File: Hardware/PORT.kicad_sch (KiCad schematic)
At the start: 6 parts

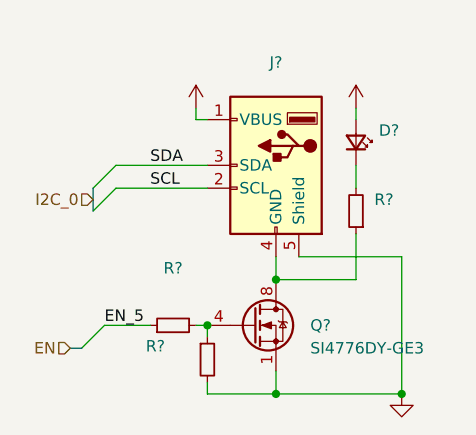
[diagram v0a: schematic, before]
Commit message: added hierrarchial labels
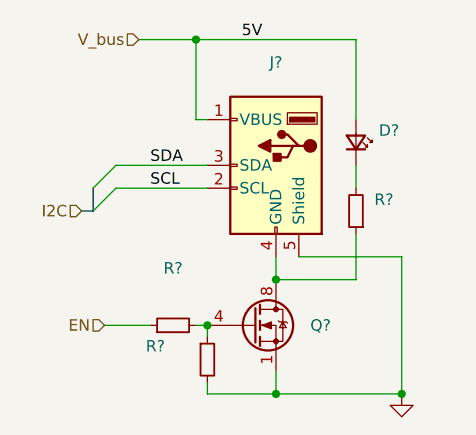
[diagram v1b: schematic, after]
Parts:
- removed D?: ~, symbol Device:LED_Small
- removed J?: ~, symbol Connector:USB_A
- removed Q?: SI4776DY-GE3, symbol Transistor_FET:Si4162DY
- removed R? (x3): ~, symbol Device:R_Small
- added D?: (no value), symbol Device:LED_Small
- added J?: (no value), symbol Connector:USB_A
- added Q?: (no value), symbol Transistor_FET:Si4162DY
- added R? (x3): (no value), symbol Device:R_Small
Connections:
- net EN: now also R?.1
- net GND: now also J?.5 (Shield), Q?.1 (S), Q?.2 (S), Q?.3 (S), R?.2
- net SCL: now also J?.2 (SCL)
- net SDA: now also J?.3 (SDA)
- new net: D?.1 (K), R?.2
- new net: Q?.4 (G), R?.1, R?.2
- new net: J?.4 (GND), Q?.5 (D), Q?.6 (D), Q?.7 (D), Q?.8 (D), R?.1
- new net V_bus: D?.2 (A), J?.1 (VBUS)
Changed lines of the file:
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@@
   (junction (at 101.6 60.96) (diameter 0) (color 0 0 0 0)
   )
+  (junction (at 92.71 34.29) (diameter 0) (color 0 0 0 0)
+  )
   (junction (at 93.98 66.04) (diameter 0) (color 0 0 0 0)
   )
@@
     (stroke (width 0) (type default) (color 0 0 0 0))
   )
-  (bus_entry (at 82.55 66.04) (size -2.54 2.54)
-    (stroke (width 0) (type default) (color 0 0 0 0))
-  )
-  (wire (pts (xy 110.49 41.91) (xy 110.49 43.18))
+  (wire (pts (xy 110.49 34.29) (xy 92.71 34.29))
+    (stroke (width 0) (type default) (color 0 0 0 0))
+  )
+  (wire (pts (xy 110.49 34.29) (xy 110.49 43.18))
     (stroke (width 0) (type default) (color 0 0 0 0))
   )
@@
     (stroke (width 0) (type default) (color 0 0 0 0))
   )
+  (wire (pts (xy 92.71 34.29) (xy 86.36 34.29))
+    (stroke (width 0) (type default) (color 0 0 0 0))
+  )
   (wire (pts (xy 101.6 73.66) (xy 115.57 73.66))
     (stroke (width 0) (type default) (color 0 0 0 0))
@@
     (stroke (width 0) (type default) (color 0 0 0 0))
   )
-  (wire (pts (xy 92.71 41.91) (xy 92.71 43.18))
+  (wire (pts (xy 92.71 34.29) (xy 92.71 43.18))
     (stroke (width 0) (type default) (color 0 0 0 0))
   )
@@
     (stroke (width 0) (type default) (color 0 0 0 0))
   )
-  (bus (pts (xy 78.74 68.58) (xy 80.01 68.58))
+  (bus (pts (xy 80.01 53.34) (xy 81.28 53.34))
     (stroke (width 0) (type default) (color 0 0 0 0))
   )
@@
     (effects (font (size 1.27 1.27)) (justify left bottom))
   )
-  (label "EN_5" (at 82.55 66.04 0)
-    (effects (font (size 1.27 1.27)) (justify left bottom))
-  )
   (label "SCL" (at 87.6284 50.8 0)
     (effects (font (size 1.27 1.27)) (justify left bottom))
   )
-  (hierarchical_label "I2C_0" (shape input) (at 81.28 52.07 180)
+  (label "5V" (at 97.79 34.29 0)
+    (effects (font (size 1.27 1.27)) (justify left bottom))
+  )
+  (hierarchical_label "V_bus" (shape input) (at 86.36 34.29 180)
     (effects (font (size 1.27 1.27)) (justify right))
   )
-  (hierarchical_label "EN" (shape input) (at 78.74 68.58 180)
+  (hierarchical_label "EN" (shape input) (at 82.55 66.04 180)
     (effects (font (size 1.27 1.27)) (justify right))
   )
-  (symbol (lib_id "power:+5V") (at 110.49 41.91 0) (unit 1)
-    (in_bom yes) (on_board yes)
-    (property "Reference" "#PWR?" (id 0) (at 110.49 45.72 0)
-      (effects (font (size 1.27 1.27)) hide)
-    )
-    (property "Value" "~" (id 1) (at 111.76 40.64 0)
-      (effects (font (size 1.27 1.27)) (justify left))
-    )
-    (property "Footprint" "" (id 2) (at 110.49 41.91 0)
-      (effects (font (size 1.27 1.27)) hide)
-    )
-    (property "Datasheet" "" (id 3) (at 110.49 41.91 0)
-      (effects (font (size 1.27 1.27)) hide)
-    )
-    (pin "1")
+  (hierarchical_label "I2C" (shape input) (at 80.01 53.34 180)
+    (effects (font (size 1.27 1.27)) (justify right))
+  )
+  (symbol (lib_id "Device:LED_Small") (at 110.49 45.72 270) (mirror x) (unit 1)
+    (in_bom yes) (on_board yes) (fields_autoplaced)
+    (property "Reference" "D?" (id 0) (at 113.03 44.3864 90)
+      (effects (font (size 1.27 1.27)) (justify left))
+    )
+    (property "Value" "" (id 1) (at 113.03 46.9264 90)
+      (effects (font (size 1.27 1.27)) (justify left))
+    )
+    (property "Footprint" "" (id 2) (at 110.49 45.72 90)
+      (effects (font (size 1.27 1.27)) hide)
+    )
+    (property "Datasheet" "~" (id 3) (at 110.49 45.72 90)
+      (effects (font (size 1.27 1.27)) hide)
+    )
+    (pin "1")
+    (pin "2")
   )
   (symbol (lib_id "Device:R_Small") (at 93.98 69.85 0) (unit 1)
@@
       (effects (font (size 1.27 1.27)) (justify left))
     )
-    (property "Value" "~" (id 1) (at 87.1354 70.8955 0)
+    (property "Value" "" (id 1) (at 87.1354 70.8955 0)
       (effects (font (size 1.27 1.27)) (justify left))
     )
@@
     (pin "2")
   )
-  (symbol (lib_id "Device:R_Small") (at 90.17 66.04 90) (unit 1)
+  (symbol (lib_id "power:GND") (at 115.57 73.66 0) (unit 1)
+    (in_bom yes) (on_board yes)
+    (property "Reference" "#PWR?" (id 0) (at 115.57 80.01 0)
+      (effects (font (size 1.27 1.27)) hide)
+    )
+    (property "Value" "" (id 1) (at 118.11 73.66 0))
+    (property "Footprint" "" (id 2) (at 115.57 73.66 0)
+      (effects (font (size 1.27 1.27)) hide)
+    )
+    (property "Datasheet" "" (id 3) (at 115.57 73.66 0)
+      (effects (font (size 1.27 1.27)) hide)
+    )
+    (pin "1")
+  )
+  (symbol (lib_id "Device:R_Small") (at 110.49 53.34 180) (unit 1)
     (in_bom yes) (on_board yes) (fields_autoplaced)
-    (property "Reference" "R?" (id 0) (at 90.17 59.69 90))
-    (property "Value" "~" (id 1) (at 90.17 62.23 90))
-    (property "Footprint" "" (id 2) (at 90.17 66.04 0)
-      (effects (font (size 1.27 1.27)) hide)
-    )
-    (property "Datasheet" "~" (id 3) (at 90.17 66.04 0)
-      (effects (font (size 1.27 1.27)) hide)
-    )
-    (pin "1")
-    (pin "2")
-  )
-  (symbol (lib_name "USB_A_1") (lib_id "Connector:USB_A") (at 101.6 48.26 0) (mirror y) (unit 1)
-    (in_bom yes) (on_board yes)
-    (property "Reference" "J?" (id 0) (at 101.6 36.83 0))
-    (property "Value" "~" (id 1) (at 101.6 39.37 0))
-    (property "Footprint" "" (id 2) (at 97.79 49.53 0)
-      (effects (font (size 1.27 1.27)) hide)
-    )
-    (property "Datasheet" " ~" (id 3) (at 97.79 49.53 0)
-      (effects (font (size 1.27 1.27)) hide)
-    )
-    (pin "1")
-    (pin "2")
-    (pin "3")
-    (pin "4")
-    (pin "5")
-  )
-  (symbol (lib_id "power:+5V") (at 92.71 41.91 0) (unit 1)
-    (in_bom yes) (on_board yes)
-    (property "Reference" "#PWR?" (id 0) (at 92.71 45.72 0)
-      (effects (font (size 1.27 1.27)) hide)
-    )
-    (property "Value" "~" (id 1) (at 86.36 40.64 0)
-      (effects (font (size 1.27 1.27)) (justify left))
-    )
-    (property "Footprint" "" (id 2) (at 92.71 41.91 0)
-      (effects (font (size 1.27 1.27)) hide)
-    )
-    (property "Datasheet" "" (id 3) (at 92.71 41.91 0)
-      (effects (font (size 1.27 1.27)) hide)
-    )
-    (pin "1")
+    (property "Reference" "R?" (id 0) (at 112.5301 52.0699 0)
+      (effects (font (size 1.27 1.27)) (justify right))
+    )
+    (property "Value" "" (id 1) (at 112.5301 54.6099 0)
+      (effects (font (size 1.27 1.27)) (justify right))
+    )
+    (property "Footprint" "" (id 2) (at 110.49 53.34 0)
+      (effects (font (size 1.27 1.27)) hide)
+    )
+    (property "Datasheet" "~" (id 3) (at 110.49 53.34 0)
+      (effects (font (size 1.27 1.27)) hide)
+    )
+    (pin "1")
+    (pin "2")
   )
   (symbol (lib_id "Transistor_FET:Si4162DY") (at 99.06 66.04 0) (unit 1)
@@
       (effects (font (size 1.27 1.27)) (justify left))
     )
-    (property "Value" "SI4776DY-GE3" (id 1) (at 105.41 68.58 0)
+    (property "Value" "" (id 1) (at 105.41 68.58 0)
       (effects (font (size 1.27 1.27)) (justify left))
     )
@@
     (pin "8")
   )
-  (symbol (lib_id "Device:R_Small") (at 110.49 53.34 180) (unit 1)
+  (symbol (lib_id "Device:R_Small") (at 90.17 66.04 90) (unit 1)
     (in_bom yes) (on_board yes) (fields_autoplaced)
-    (property "Reference" "R?" (id 0) (at 112.5301 52.0699 0)
-      (effects (font (size 1.27 1.27)) (justify right))
-    )
-    (property "Value" "~" (id 1) (at 112.5301 54.6099 0)
-      (effects (font (size 1.27 1.27)) (justify right))
-    )
-    (property "Footprint" "" (id 2) (at 110.49 53.34 0)
-      (effects (font (size 1.27 1.27)) hide)
-    )
-    (property "Datasheet" "~" (id 3) (at 110.49 53.34 0)
-      (effects (font (size 1.27 1.27)) hide)
-    )
-    (pin "1")
-    (pin "2")
-  )
-  (symbol (lib_id "power:GND") (at 115.57 73.66 0) (unit 1)
-    (in_bom yes) (on_board yes)
-    (property "Reference" "#PWR?" (id 0) (at 115.57 80.01 0)
-      (effects (font (size 1.27 1.27)) hide)
-    )
-    (property "Value" "~" (id 1) (at 118.11 73.66 0))
-    (property "Footprint" "" (id 2) (at 115.57 73.66 0)
-      (effects (font (size 1.27 1.27)) hide)
-    )
-    (property "Datasheet" "" (id 3) (at 115.57 73.66 0)
-      (effects (font (size 1.27 1.27)) hide)
-    )
-    (pin "1")
-  )
-  (symbol (lib_id "Device:LED_Small") (at 110.49 45.72 270) (mirror x) (unit 1)
-    (in_bom yes) (on_board yes) (fields_autoplaced)
-    (property "Reference" "D?" (id 0) (at 113.03 44.3864 90)
-      (effects (font (size 1.27 1.27)) (justify left))
-    )
-    (property "Value" "~" (id 1) (at 113.03 46.9264 90)
-      (effects (font (size 1.27 1.27)) (justify left))
-    )
-    (property "Footprint" "" (id 2) (at 110.49 45.72 90)
-      (effects (font (size 1.27 1.27)) hide)
-    )
-    (property "Datasheet" "~" (id 3) (at 110.49 45.72 90)
-      (effects (font (size 1.27 1.27)) hide)
-    )
-    (pin "1")
-    (pin "2")
+    (property "Reference" "R?" (id 0) (at 90.17 59.69 90))
+    (property "Value" "" (id 1) (at 90.17 62.23 90))
+    (property "Footprint" "" (id 2) (at 90.17 66.04 0)
+      (effects (font (size 1.27 1.27)) hide)
+    )
+    (property "Datasheet" "~" (id 3) (at 90.17 66.04 0)
+      (effects (font (size 1.27 1.27)) hide)
+    )
+    (pin "1")
+    (pin "2")
+  )
+  (symbol (lib_name "USB_A_1") (lib_id "Connector:USB_A") (at 101.6 48.26 0) (mirror y) (unit 1)
+    (in_bom yes) (on_board yes)
+    (property "Reference" "J?" (id 0) (at 101.6 36.83 0))
+    (property "Value" "" (id 1) (at 101.6 39.37 0))
+    (property "Footprint" "" (id 2) (at 97.79 49.53 0)
+      (effects (font (size 1.27 1.27)) hide)
+    )
+    (property "Datasheet" " ~" (id 3) (at 97.79 49.53 0)
+      (effects (font (size 1.27 1.27)) hide)
+    )
+    (pin "1")
+    (pin "2")
+    (pin "3")
+    (pin "4")
+    (pin "5")
   )
 )

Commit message: cleaned up busses
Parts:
- D?: value (none) -> GLED
- J?: value (none) -> USB
- Q?: value (none) -> SI4776DY-GE3
- R?: value (none) -> 1Meg
- R? (x2): value (none) -> 1k
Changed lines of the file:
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@@
   (junction (at 101.6 73.66) (diameter 0) (color 0 0 0 0)
-  )
-  (bus_entry (at 83.82 48.26) (size -2.54 2.54)
-    (stroke (width 0) (type default) (color 0 0 0 0))
-  )
-  (bus_entry (at 83.82 50.8) (size -2.54 2.54)
-    (stroke (width 0) (type default) (color 0 0 0 0))
   )
   (wire (pts (xy 110.49 34.29) (xy 92.71 34.29))
@@
     (stroke (width 0) (type default) (color 0 0 0 0))
   )
-  (bus (pts (xy 80.01 53.34) (xy 81.28 53.34))
-    (stroke (width 0) (type default) (color 0 0 0 0))
-  )
   (wire (pts (xy 82.55 66.04) (xy 87.63 66.04))
     (stroke (width 0) (type default) (color 0 0 0 0))
@@
   )
   (wire (pts (xy 110.49 60.96) (xy 101.6 60.96))
-    (stroke (width 0) (type default) (color 0 0 0 0))
-  )
-  (bus (pts (xy 81.28 50.8) (xy 81.28 53.34))
     (stroke (width 0) (type default) (color 0 0 0 0))
   )
@@
     (effects (font (size 1.27 1.27)) (justify right))
   )
+  (hierarchical_label "SCL" (shape input) (at 83.82 50.8 180)
+    (effects (font (size 1.27 1.27)) (justify right))
+  )
   (hierarchical_label "EN" (shape input) (at 82.55 66.04 180)
     (effects (font (size 1.27 1.27)) (justify right))
   )
-  (hierarchical_label "I2C" (shape input) (at 80.01 53.34 180)
+  (hierarchical_label "SDA" (shape input) (at 83.82 48.26 180)
     (effects (font (size 1.27 1.27)) (justify right))
   )
@@
       (effects (font (size 1.27 1.27)) (justify left))
     )
-    (property "Value" "" (id 1) (at 113.03 46.9264 90)
+    (property "Value" "GLED" (id 1) (at 113.03 46.9264 90)
       (effects (font (size 1.27 1.27)) (justify left))
     )
@@
       (effects (font (size 1.27 1.27)) (justify left))
     )
-    (property "Value" "" (id 1) (at 87.1354 70.8955 0)
+    (property "Value" "1Meg" (id 1) (at 87.1354 70.8955 0)
       (effects (font (size 1.27 1.27)) (justify left))
     )
@@
       (effects (font (size 1.27 1.27)) hide)
     )
-    (property "Value" "" (id 1) (at 118.11 73.66 0))
+    (property "Value" "~" (id 1) (at 118.11 73.66 0))
     (property "Footprint" "" (id 2) (at 115.57 73.66 0)
       (effects (font (size 1.27 1.27)) hide)
@@
       (effects (font (size 1.27 1.27)) (justify right))
     )
-    (property "Value" "" (id 1) (at 112.5301 54.6099 0)
+    (property "Value" "1k" (id 1) (at 112.5301 54.6099 0)
       (effects (font (size 1.27 1.27)) (justify right))
     )
@@
       (effects (font (size 1.27 1.27)) (justify left))
     )
-    (property "Value" "" (id 1) (at 105.41 68.58 0)
+    (property "Value" "SI4776DY-GE3" (id 1) (at 105.41 68.58 0)
       (effects (font (size 1.27 1.27)) (justify left))
     )
@@
     (in_bom yes) (on_board yes) (fields_autoplaced)
     (property "Reference" "R?" (id 0) (at 90.17 59.69 90))
-    (property "Value" "" (id 1) (at 90.17 62.23 90))
+    (property "Value" "1k" (id 1) (at 90.17 62.23 90))
     (property "Footprint" "" (id 2) (at 90.17 66.04 0)
       (effects (font (size 1.27 1.27)) hide)
@@
     (in_bom yes) (on_board yes)
     (property "Reference" "J?" (id 0) (at 101.6 36.83 0))
-    (property "Value" "" (id 1) (at 101.6 39.37 0))
+    (property "Value" "USB" (id 1) (at 101.6 39.37 0))
     (property "Footprint" "" (id 2) (at 97.79 49.53 0)
       (effects (font (size 1.27 1.27)) hide)

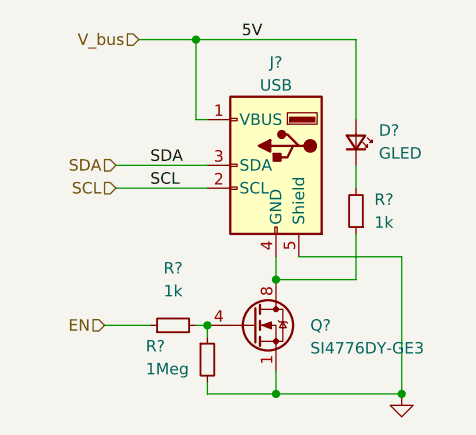
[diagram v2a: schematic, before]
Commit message: changed Schematic and added RTC
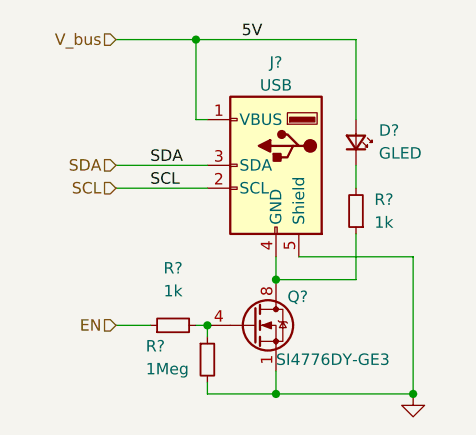
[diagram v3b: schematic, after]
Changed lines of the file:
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@@
   (junction (at 93.98 66.04) (diameter 0) (color 0 0 0 0)
   )
-  (junction (at 115.57 73.66) (diameter 0) (color 0 0 0 0)
+  (junction (at 116.84 73.66) (diameter 0) (color 0 0 0 0)
   )
   (junction (at 101.6 73.66) (diameter 0) (color 0 0 0 0)
@@
     (stroke (width 0) (type default) (color 0 0 0 0))
   )
-  (wire (pts (xy 92.71 34.29) (xy 86.36 34.29))
-    (stroke (width 0) (type default) (color 0 0 0 0))
-  )
-  (wire (pts (xy 101.6 73.66) (xy 115.57 73.66))
+  (wire (pts (xy 92.71 34.29) (xy 83.82 34.29))
     (stroke (width 0) (type default) (color 0 0 0 0))
   )
@@
     (stroke (width 0) (type default) (color 0 0 0 0))
   )
-  (wire (pts (xy 115.57 58.42) (xy 104.14 58.42))
+  (wire (pts (xy 116.84 58.42) (xy 104.14 58.42))
     (stroke (width 0) (type default) (color 0 0 0 0))
   )
-  (wire (pts (xy 115.57 73.66) (xy 115.57 58.42))
+  (wire (pts (xy 116.84 73.66) (xy 116.84 58.42))
     (stroke (width 0) (type default) (color 0 0 0 0))
   )
@@
     (stroke (width 0) (type default) (color 0 0 0 0))
   )
-  (wire (pts (xy 82.55 66.04) (xy 87.63 66.04))
+  (wire (pts (xy 83.82 66.04) (xy 87.63 66.04))
     (stroke (width 0) (type default) (color 0 0 0 0))
   )
@@
   )
   (wire (pts (xy 93.98 73.66) (xy 101.6 73.66))
+    (stroke (width 0) (type default) (color 0 0 0 0))
+  )
+  (wire (pts (xy 101.6 73.66) (xy 116.84 73.66))
     (stroke (width 0) (type default) (color 0 0 0 0))
   )
@@
     (effects (font (size 1.27 1.27)) (justify left bottom))
   )
-  (hierarchical_label "V_bus" (shape input) (at 86.36 34.29 180)
+  (hierarchical_label "V_bus" (shape input) (at 83.82 34.29 180)
     (effects (font (size 1.27 1.27)) (justify right))
   )
@@
     (effects (font (size 1.27 1.27)) (justify right))
   )
-  (hierarchical_label "EN" (shape input) (at 82.55 66.04 180)
+  (hierarchical_label "EN" (shape input) (at 83.82 66.04 180)
     (effects (font (size 1.27 1.27)) (justify right))
   )
@@
     (pin "2")
   )
-  (symbol (lib_id "power:GND") (at 115.57 73.66 0) (unit 1)
+  (symbol (lib_id "power:GND") (at 116.84 73.66 0) (unit 1)
     (in_bom yes) (on_board yes)
-    (property "Reference" "#PWR?" (id 0) (at 115.57 80.01 0)
+    (property "Reference" "#PWR?" (id 0) (at 116.84 80.01 0)
       (effects (font (size 1.27 1.27)) hide)
     )
-    (property "Value" "~" (id 1) (at 118.11 73.66 0))
-    (property "Footprint" "" (id 2) (at 115.57 73.66 0)
+    (property "Value" "~" (id 1) (at 119.38 73.66 0))
+    (property "Footprint" "" (id 2) (at 116.84 73.66 0)
       (effects (font (size 1.27 1.27)) hide)
     )
-    (property "Datasheet" "" (id 3) (at 115.57 73.66 0)
+    (property "Datasheet" "" (id 3) (at 116.84 73.66 0)
       (effects (font (size 1.27 1.27)) hide)
     )
@@
   (symbol (lib_id "Transistor_FET:Si4162DY") (at 99.06 66.04 0) (unit 1)
     (in_bom yes) (on_board yes)
-    (property "Reference" "Q?" (id 0) (at 105.41 66.04 0)
+    (property "Reference" "Q?" (id 0) (at 102.87 62.865 0)
       (effects (font (size 1.27 1.27)) (justify left))
     )
-    (property "Value" "SI4776DY-GE3" (id 1) (at 105.41 68.58 0)
+    (property "Value" "SI4776DY-GE3" (id 1) (at 101.6 69.85 0)
       (effects (font (size 1.27 1.27)) (justify left))
     )
